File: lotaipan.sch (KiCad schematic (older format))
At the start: 70 parts, among them J1 SMA_through, J2 SMA_through, P1 47309-2651_uSD_slot, P2 CONN_01X20, P3 CONN_01X25, P4 USB_OTG, Q1 MOS_N_SGD, U1 RN2483, U2 STM32F405R, U3 MCP1703, U4 MCP73831-2ACI/0T, U5 MIC94091YC6, U6 MIC94091YC6, Y1 12MHz, Y2 32kHz

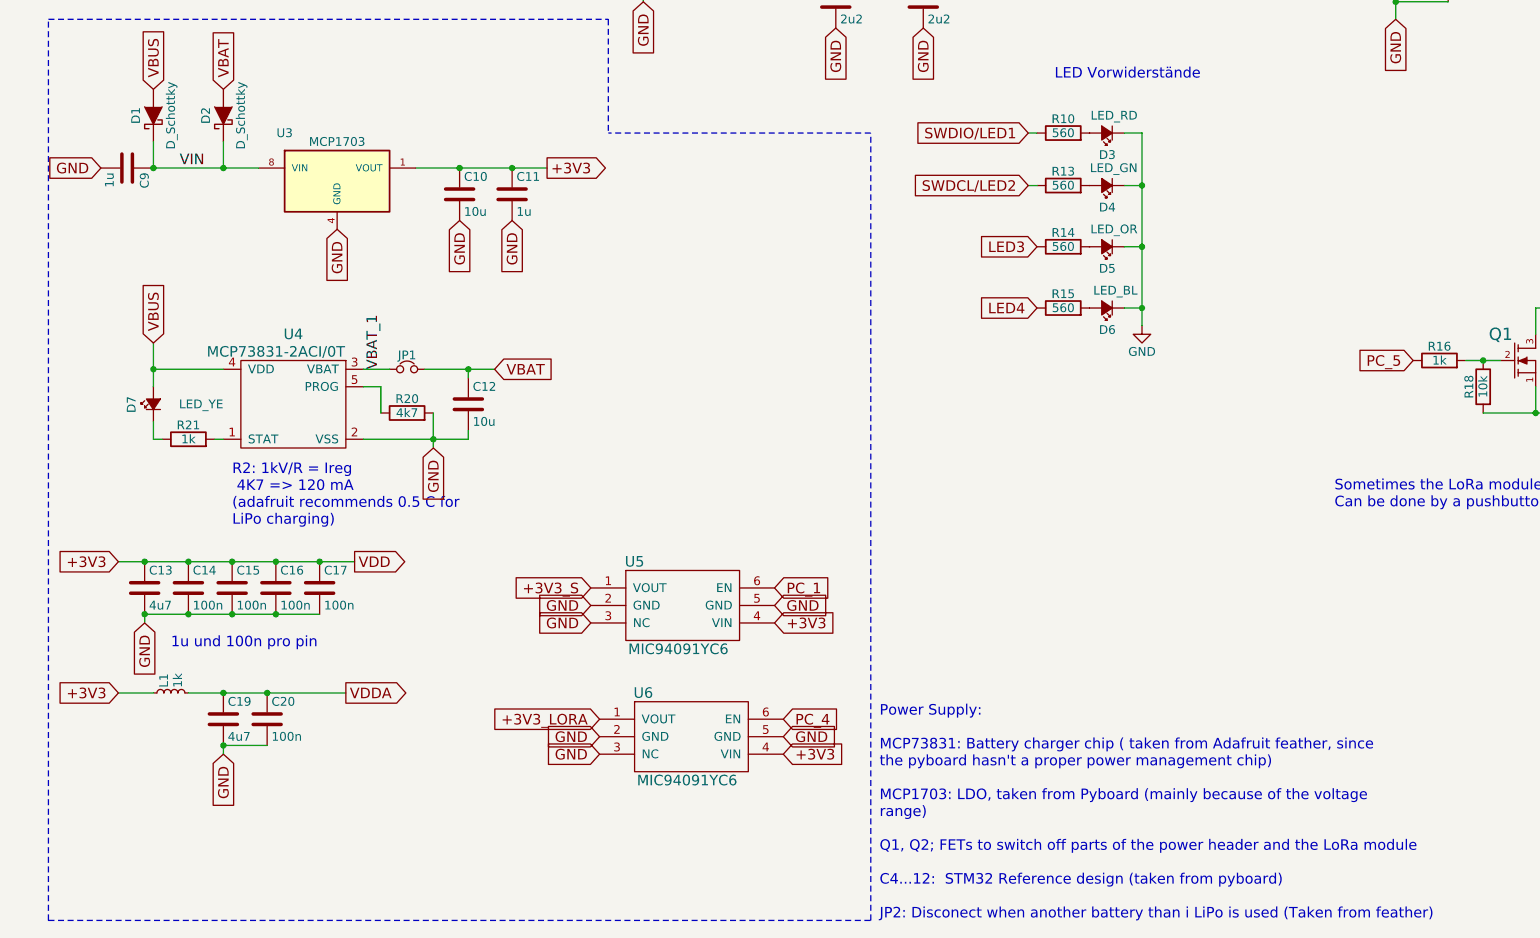
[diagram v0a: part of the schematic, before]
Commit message: Notes in schematics
Layout schould be updated
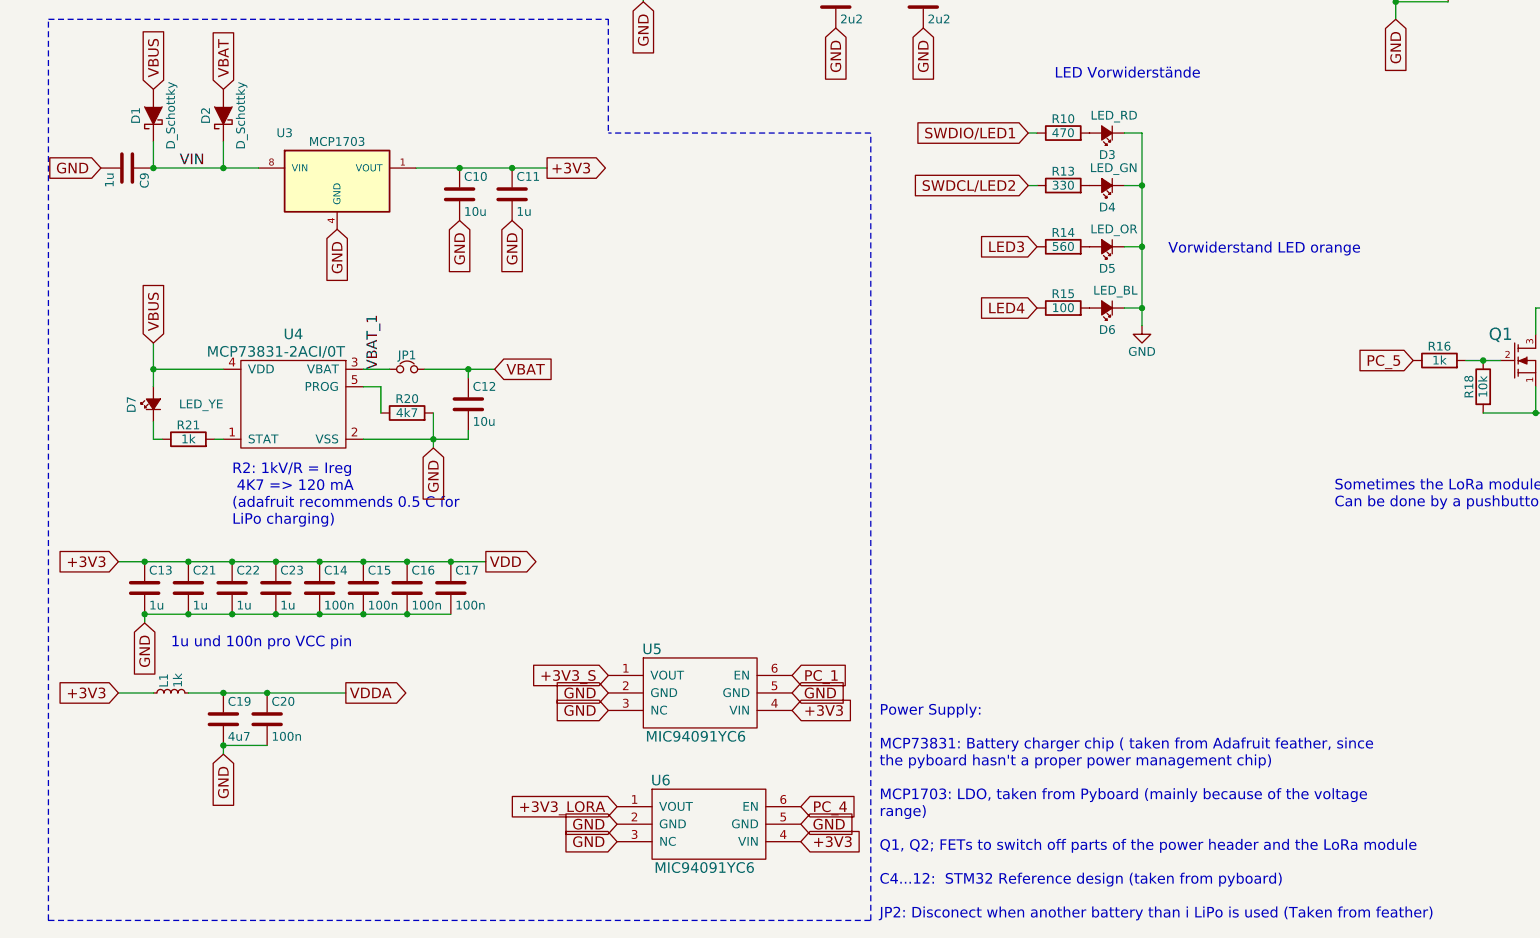
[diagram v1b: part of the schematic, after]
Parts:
- added C21, C22, C23: 1u, Capacitors_SMD:C_0402, symbol C
- C13: value 4u7 -> 1u
- R10: value 560 -> 470
- R13: value 560 -> 330
- R15: value 560 -> 100
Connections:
- net +3V3: now also C21.1, C22.1, C23.1
- net GND: now also C21.2, C22.2, C23.2
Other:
- note added: "1u und 100n pro VCC pin"
- note added: "Vorwiderstand LED orange"
- note removed: "1u und 100n pro pin"
- moved on the sheet: C14, C15, C16, C17, U5, U6
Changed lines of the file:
@@
 EESchema Schematic File Version 2
-LIBS:ab2_7segment
-LIBS:ab2_audio
-LIBS:ab2_buffer
-LIBS:ab2_capacitor
-LIBS:ab2_connectivity
-LIBS:ab2_dac
-LIBS:ab2_diode
-LIBS:ab2_gpio_expansion
-LIBS:ab2_header
-LIBS:ab2_idc
-LIBS:ab2_inductor
-LIBS:ab2_input_devices
-LIBS:ab2_jumper
-LIBS:ab2_lcd
-LIBS:ab2_led
-LIBS:ab2_memory
-LIBS:ab2_opamp
-LIBS:ab2_pot
-LIBS:ab2_power
-LIBS:ab2_regulator
-LIBS:ab2_relay
-LIBS:ab2_resistor
-LIBS:ab2_sensor
-LIBS:ab2_stepper
-LIBS:ab2_supply
-LIBS:ab2_terminal_block
-LIBS:ab2_test
-LIBS:ab2_transistor
-LIBS:ab2_uC
-LIBS:ab2_usb
-LIBS:ab2_xtal
-LIBS:T_various
-LIBS:w_analog
-LIBS:w_connectors
-LIBS:w_device
-LIBS:w_logic
-LIBS:w_memory
-LIBS:w_microcontrollers
-LIBS:w_opto
-LIBS:w_relay
-LIBS:w_rtx
-LIBS:w_transistor
-LIBS:w_vacuum
 LIBS:Symbols_DCDC-ACDC-Converter_RevC_20Jul2012
 LIBS:Symbols_EN60617_13Mar2013
@@
 P 1100 9200
 F 0 "C13" H 1125 9300 50  0000 L CNN
-F 1 "4u7" H 1125 9100 50  0000 L CNN
+F 1 "1u" H 1125 9100 50  0000 L CNN
 F 2 "Capacitors_SMD:C_0402" H 1138 9050 50  0001 C CNN
 F 3 "" H 1100 9200 50  0000 C CNN
@@
 L C C15
 U 1 1 5710F017
-P 1600 9200
-F 0 "C15" H 1625 9300 50  0000 L CNN
-F 1 "100n" H 1625 9100 50  0000 L CNN
-F 2 "Capacitors_SMD:C_0402" H 1638 9050 50  0001 C CNN
-F 3 "" H 1600 9200 50  0000 C CNN
-	1    1600 9200
+P 2350 9200
+F 0 "C15" H 2375 9300 50  0000 L CNN
+F 1 "100n" H 2375 9100 50  0000 L CNN
+F 2 "Capacitors_SMD:C_0402" H 2388 9050 50  0001 C CNN
+F 3 "" H 2350 9200 50  0000 C CNN
+	1    2350 9200
 	1    0    0    -1
 $EndComp
@@
 L C C16
 U 1 1 5710F057
-P 1850 9200
-F 0 "C16" H 1875 9300 50  0000 L CNN
-F 1 "100n" H 1875 9100 50  0000 L CNN
-F 2 "Capacitors_SMD:C_0402" H 1888 9050 50  0001 C CNN
-F 3 "" H 1850 9200 50  0000 C CNN
-	1    1850 9200
+P 2600 9200
+F 0 "C16" H 2625 9300 50  0000 L CNN
+F 1 "100n" H 2625 9100 50  0000 L CNN
+F 2 "Capacitors_SMD:C_0402" H 2638 9050 50  0001 C CNN
+F 3 "" H 2600 9200 50  0000 C CNN
+	1    2600 9200
 	1    0    0    -1
 $EndComp
@@
 L C C17
 U 1 1 5710F0A2
+P 2850 9200
+F 0 "C17" H 2875 9300 50  0000 L CNN
+F 1 "100n" H 2875 9100 50  0000 L CNN
+F 2 "Capacitors_SMD:C_0402" H 2888 9050 50  0001 C CNN
+F 3 "" H 2850 9200 50  0000 C CNN
+	1    2850 9200
+	1    0    0    -1
+$EndComp
+$Comp
+L C C14
+U 1 1 5710F127
 P 2100 9200
-F 0 "C17" H 2125 9300 50  0000 L CNN
+F 0 "C14" H 2125 9300 50  0000 L CNN
 F 1 "100n" H 2125 9100 50  0000 L CNN
 F 2 "Capacitors_SMD:C_0402" H 2138 9050 50  0001 C CNN
@@
 	1    0    0    -1
 $EndComp
-$Comp
-L C C14
-U 1 1 5710F127
-P 1350 9200
-F 0 "C14" H 1375 9300 50  0000 L CNN
-F 1 "100n" H 1375 9100 50  0000 L CNN
-F 2 "Capacitors_SMD:C_0402" H 1388 9050 50  0001 C CNN
-F 3 "" H 1350 9200 50  0000 C CNN
-	1    1350 9200
-	1    0    0    -1
-$EndComp
-Wire Wire Line
-	950  9050 2300 9050
+Wire Wire Line
+	950  9050 3050 9050
 Connection ~ 1100 9050
-Connection ~ 1350 9050
-Connection ~ 1600 9050
-Connection ~ 1850 9050
-Wire Wire Line
-	1100 9350 2100 9350
-Connection ~ 1350 9350
-Connection ~ 1600 9350
-Connection ~ 1850 9350
-Text GLabel 2300 9050 2    60   Output ~ 0
+Connection ~ 2100 9050
+Connection ~ 2350 9050
+Connection ~ 2600 9050
+Wire Wire Line
+	1100 9350 2850 9350
+Connection ~ 2100 9350
+Connection ~ 2350 9350
+Connection ~ 2600 9350
+Text GLabel 3050 9050 2    60   Output ~ 0
 VDD
-Connection ~ 2100 9050
+Connection ~ 2850 9050
 Connection ~ 1100 9350
 Text GLabel 950  9800 0    60   Input ~ 0
@@
 $EndComp
 $Comp
-L GND-RESCUE-LoRa_Stuff #PWR01
+L GND-RESCUE-LoRa_Stuff #PWR3
 U 1 1 5711B1EE
 P 11600 6900
-F 0 "#PWR01" H 11600 6650 50  0001 C CNN
+F 0 "#PWR3" H 11600 6650 50  0001 C CNN
 F 1 "GND" H 11600 6750 50  0000 C CNN
 F 2 "" H 11600 6900 50  0000 C CNN
@@
 $EndComp
 $Comp
-L GND-RESCUE-LoRa_Stuff #PWR02
+L GND-RESCUE-LoRa_Stuff #PWR2
 U 1 1 5711B53D
 P 11200 6700
-F 0 "#PWR02" H 11200 6450 50  0001 C CNN
+F 0 "#PWR2" H 11200 6450 50  0001 C CNN
 F 1 "GND" H 11200 6550 50  0000 C CNN
 F 2 "" H 11200 6700 50  0000 C CNN
@@
 $EndComp
 $Comp
-L GND-RESCUE-LoRa_Stuff #PWR03
+L GND-RESCUE-LoRa_Stuff #PWR1
 U 1 1 5711F4EF
 P 6800 7700
-F 0 "#PWR03" H 6800 7450 50  0001 C CNN
+F 0 "#PWR1" H 6800 7450 50  0001 C CNN
 F 1 "GND" H 6800 7550 50  0000 C CNN
 F 2 "" H 6800 7700 50  0000 C CNN
@@
 P 6350 6900
 F 0 "R13" V 6430 6900 50  0000 C CNN
-F 1 "560" V 6350 6900 50  0000 C CNN
+F 1 "330" V 6350 6900 50  0000 C CNN
 F 2 "Resistors_SMD:R_0402" V 6280 6900 50  0001 C CNN
 F 3 "" H 6350 6900 50  0000 C CNN
@@
 Text GLabel 13900 5200 0    60   Input ~ 0
 PC_0
-Text GLabel 4700 9200 2    60   Input ~ 0
+Text GLabel 4800 9700 2    60   Input ~ 0
 PC_1
 Text GLabel 13900 5300 0    60   Input ~ 0
@@
 Wire Notes Line
 	550  11100 550  5950
-Text GLabel 3650 9200 0    60   Input ~ 0
+Text GLabel 3750 9700 0    60   Input ~ 0
 +3V3_S
 $Comp
@@
 Connection ~ 9050 8200
 Connection ~ 8750 7900
-Text GLabel 3700 9950 0    60   Input ~ 0
+Text GLabel 3800 10450 0    60   Input ~ 0
 +3V3_LORA
-Text GLabel 4750 10150 2    60   Input ~ 0
+Text GLabel 4850 10650 2    60   Input ~ 0
 +3V3
-Text GLabel 4750 9950 2    60   Input ~ 0
+Text GLabel 4850 10450 2    60   Input ~ 0
 PC_4
 Wire Notes Line
@@
 P 6350 6600
 F 0 "R10" V 6430 6600 50  0000 C CNN
-F 1 "560" V 6350 6600 50  0000 C CNN
+F 1 "470" V 6350 6600 50  0000 C CNN
 F 2 "Resistors_SMD:R_0402" V 6280 6600 50  0001 C CNN
 F 3 "" H 6350 6600 50  0000 C CNN
@@
 P 6350 7600
 F 0 "R15" V 6430 7600 50  0000 C CNN
-F 1 "560" V 6350 7600 50  0000 C CNN
+F 1 "100" V 6350 7600 50  0000 C CNN
 F 2 "Resistors_SMD:R_0402" V 6280 7600 50  0001 C CNN
 F 3 "" H 6350 7600 50  0000 C CNN
@@
 L MIC94091YC6 U6
 U 1 1 57D57CD7
-P 3700 9950
-F 0 "U6" H 3950 10100 60  0000 C CNN
-F 1 "MIC94091YC6" H 4200 9600 60  0000 C CNN
-F 2 "TO_SOT_Packages_SMD:SC-70-6" H 4550 8400 60  0001 C CNN
-F 3 "" H 4550 8400 60  0001 C CNN
-	1    3700 9950
+P 3800 10450
+F 0 "U6" H 4050 10600 60  0000 C CNN
+F 1 "MIC94091YC6" H 4300 10100 60  0000 C CNN
+F 2 "TO_SOT_Packages_SMD:SC-70-6" H 4650 8900 60  0001 C CNN
+F 3 "" H 4650 8900 60  0001 C CNN
+	1    3800 10450
 	1    0    0    -1
 $EndComp
@@
 L MIC94091YC6 U5
 U 1 1 57D57F90
-P 3650 9200
-F 0 "U5" H 3900 9350 60  0000 C CNN
-F 1 "MIC94091YC6" H 4150 8850 60  0000 C CNN
-F 2 "TO_SOT_Packages_SMD:SC-70-6" H 4500 7650 60  0001 C CNN
-F 3 "" H 4500 7650 60  0001 C CNN
-	1    3650 9200
-	1    0    0    -1
-$EndComp
-Text GLabel 3700 10050 0    60   Input ~ 0
-GND
-Text GLabel 3700 10150 0    60   Input ~ 0
-GND
-Text GLabel 4750 10050 2    60   Input ~ 0
-GND
-Text GLabel 4700 9400 2    60   Input ~ 0
+P 3750 9700
+F 0 "U5" H 4000 9850 60  0000 C CNN
+F 1 "MIC94091YC6" H 4250 9350 60  0000 C CNN
+F 2 "TO_SOT_Packages_SMD:SC-70-6" H 4600 8150 60  0001 C CNN
+F 3 "" H 4600 8150 60  0001 C CNN
+	1    3750 9700
+	1    0    0    -1
+$EndComp
+Text GLabel 3800 10550 0    60   Input ~ 0
+GND
+Text GLabel 3800 10650 0    60   Input ~ 0
+GND
+Text GLabel 4850 10550 2    60   Input ~ 0
+GND
+Text GLabel 4800 9900 2    60   Input ~ 0
 +3V3
-Text GLabel 3650 9300 0    60   Input ~ 0
-GND
-Text GLabel 3650 9400 0    60   Input ~ 0
-GND
-Text GLabel 4700 9300 2    60   Input ~ 0
+Text GLabel 3750 9800 0    60   Input ~ 0
+GND
+Text GLabel 3750 9900 0    60   Input ~ 0
+GND
+Text GLabel 4800 9800 2    60   Input ~ 0
 GND
 Text Notes 6300 6300 0    60   ~ 0
@@
 	10700 6100 11200 6100
 Text Notes 1250 9550 0    60   ~ 0
-1u und 100n pro pin
+1u und 100n pro VCC pin
+$Comp
+L C C21
+U 1 1 57F22FFA
+P 1350 9200
+F 0 "C21" H 1375 9300 50  0000 L CNN
+F 1 "1u" H 1375 9100 50  0000 L CNN
+F 2 "Capacitors_SMD:C_0402" H 1388 9050 50  0001 C CNN
+F 3 "" H 1350 9200 50  0000 C CNN
+	1    1350 9200
+	1    0    0    -1
+$EndComp
+$Comp
+L C C22
+U 1 1 57F23852
+P 1600 9200
+F 0 "C22" H 1625 9300 50  0000 L CNN
+F 1 "1u" H 1625 9100 50  0000 L CNN
+F 2 "Capacitors_SMD:C_0402" H 1638 9050 50  0001 C CNN
+F 3 "" H 1600 9200 50  0000 C CNN
+	1    1600 9200
+	1    0    0    -1
+$EndComp
+$Comp
+L C C23
+U 1 1 57F2393F
+P 1850 9200
+F 0 "C23" H 1875 9300 50  0000 L CNN
+F 1 "1u" H 1875 9100 50  0000 L CNN
+F 2 "Capacitors_SMD:C_0402" H 1888 9050 50  0001 C CNN
+F 3 "" H 1850 9200 50  0000 C CNN
+	1    1850 9200
+	1    0    0    -1
+$EndComp
+Connection ~ 1350 9350
+Connection ~ 1600 9350
+Connection ~ 1850 9350
+Connection ~ 1850 9050
+Connection ~ 1600 9050
+Connection ~ 1350 9050
+Text Notes 6950 7300 0    60   ~ 0
+Vorwiderstand LED orange
 $EndSCHEMATC
